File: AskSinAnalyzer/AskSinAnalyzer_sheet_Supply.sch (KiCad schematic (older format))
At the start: 8 parts, among them J1 Supply, J2 USB_B_Micro, Q1 IRLML5203, U1 LM1117-3.3

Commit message: new microUSB connector
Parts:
- J2: footprint Connectors:USB_Micro-B -> myConnectors:USB_Micro
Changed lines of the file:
@@
 F 0 "J2" H 2282 4167 50  0000 C CNN
 F 1 "USB_B_Micro" H 2282 4076 50  0000 C CNN
-F 2 "Connectors:USB_Micro-B" H 2375 3650 50  0001 C CNN
+F 2 "myConnectors:USB_Micro" H 2375 3650 50  0001 C CNN
 F 3 "~" H 2375 3650 50  0001 C CNN
 	1    2225 3700

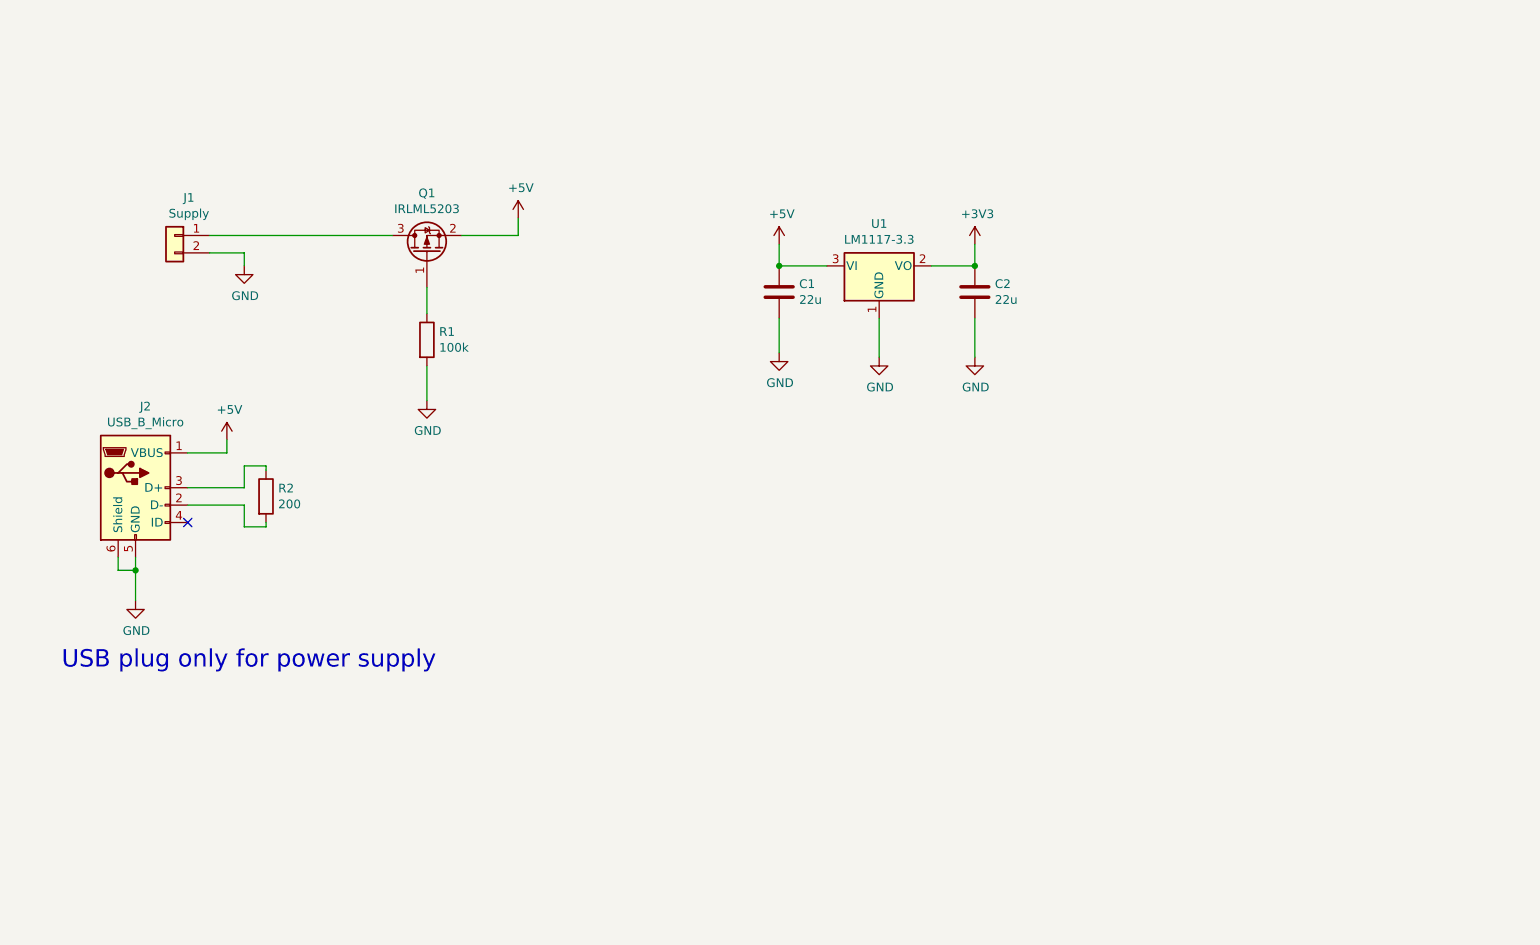
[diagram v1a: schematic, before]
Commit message: AskSinAnalyzer PCB V2.0 RC1
added a FTDI FT245 to flash and debug ESP32
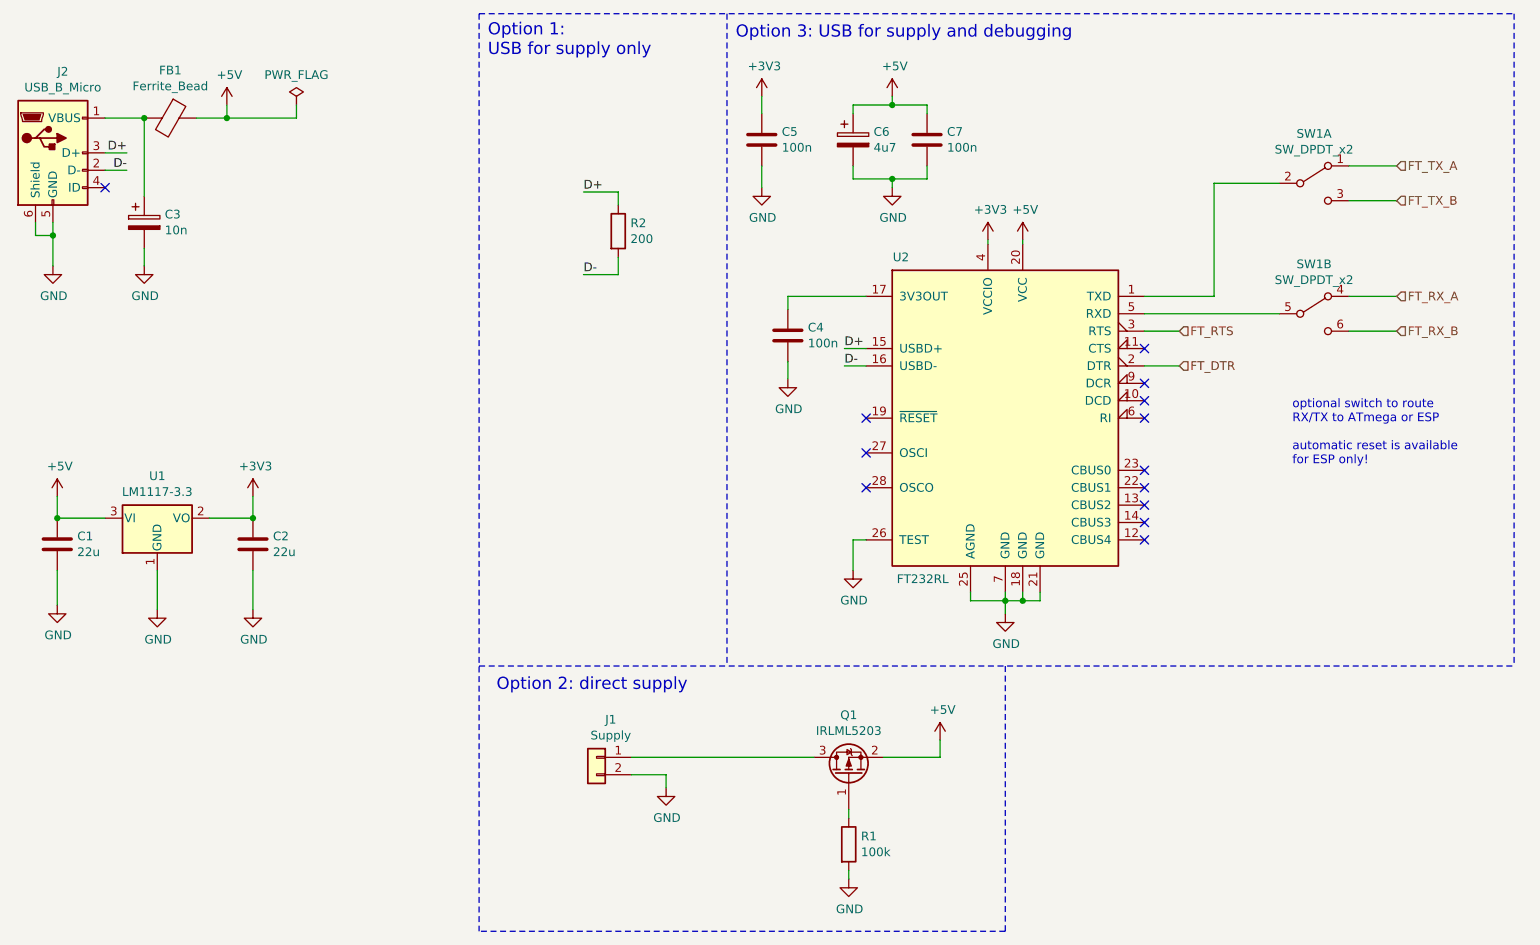
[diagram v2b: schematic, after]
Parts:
- added C3: 10n, Capacitors_SMD:C_0805_HandSoldering, symbol Device:CP
- added C4, C5: 100n, Capacitors_SMD:C_0805_HandSoldering, symbol Device:C
- added C6: 4u7, Capacitors_SMD:C_1210_HandSoldering, symbol Device:CP
- added C7: 100n, Capacitors_SMD:C_1206_HandSoldering, symbol Device:C
- added FB1: Ferrite_Bead, Resistors_SMD:R_0805_HandSoldering, symbol Device:Ferrite_Bead
- added SW1: SW_DPDT_x2, Buttons_Switches_THT:SW_CuK_JS202011CQN_DPDT_Straight, symbol Switch:SW_DPDT_x2
- added U2: FT232RL, Housings_SSOP:SSOP-28_5.3x10.2mm_Pitch0.65mm, symbol Interface_USB:FT232RL
- C1, C2: footprint Capacitors_SMD:C_1206_HandSoldering -> Capacitors_SMD:C_1210_HandSoldering
- Q1: footprint TO_SOT_Packages_SMD:SOT-23 -> TO_SOT_Packages_SMD:SOT-23_Handsoldering
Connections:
- net +3V3: now also C5.1, U2.4 (VCCIO)
- net +5V: now also C6.1, C7.1, FB1.1, U2.20 (VCC); no longer J2.1 (VBUS)
- net GND: now also C3.2, C4.2, C5.2, C6.2, C7.2, U2.18 (GND), U2.21 (GND), U2.25 (AGND), U2.26 (TEST), U2.7 (GND)
- net D-: now reaches J2.2 (D-), R2.2
- net D-: now also U2.16 (USBD-)
- net D+: now reaches J2.3 (D+), R2.1
- net D+: now also U2.15 (USBD+)
- new net: C3.1, FB1.2, J2.1 (VBUS)
- new net: SW1.2 (B), U2.1 (TXD)
- new net: C4.1, U2.17 (3V3OUT)
- new net: SW1.5 (B), U2.5 (RXD)
- new net FT_DTR: U2.2 (DTR)
- new net FT_RTS: U2.3 (RTS)
- new net FT_RX_A: SW1.4 (A)
- new net FT_RX_B: SW1.6 (C)
- new net FT_TX_A: SW1.1 (A)
- new net FT_TX_B: SW1.3 (C)
- no-connect marks 1 -> 13
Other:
- note added: "Option 1: \nUSB for supply only"
- note added: "Option 2: direct supply"
- note added: "Option 3: USB for supply and debugging\n"
- note added: "optional switch to route \nRX/TX to ATmega or ESP\n\nautomatic reset is available\nfor ESP only!\n"
- note removed: "USB plug only for power supply"
- moved on the sheet: C1, C2, J1, J2, Q1, R1, R2, U1

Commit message: AskSinAnalyzer PCB V2.0
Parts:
- C1, C2: footprint Capacitors_SMD:C_1210_HandSoldering -> Capacitors_Tantalum_SMD:CP_Tantalum_Case-B_EIA-3528-21_Hand; symbol Device:C -> Device:CP
- C3: symbol Device:CP -> Device:C
- C6: footprint Capacitors_SMD:C_1210_HandSoldering -> Capacitors_Tantalum_SMD:CP_Tantalum_Case-B_EIA-3528-21_Hand
- C7: footprint Capacitors_SMD:C_1206_HandSoldering -> Capacitors_SMD:C_0805_HandSoldering
- U2: footprint Housings_SSOP:SSOP-28_5.3x10.2mm_Pitch0.65mm -> myHousings:SSOP-28_5.3x10.2mm_Pitch0.65mm_Handsoldering
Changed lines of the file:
@@
 	6325 5900 6325 5950
 $Comp
-L Device:C C1
+L Device:CP C1
 U 1 1 5D5BA7C1
 P 1775 4025
 F 0 "C1" H 1890 4071 50  0000 L CNN
 F 1 "22u" H 1890 3980 50  0000 L CNN
-F 2 "Capacitors_SMD:C_1210_HandSoldering" H 1813 3875 50  0001 C CNN
+F 2 "Capacitors_Tantalum_SMD:CP_Tantalum_Case-B_EIA-3528-21_Hand" H 1813 3875 50  0001 C CNN
 F 3 "~" H 1775 4025 50  0001 C CNN
 	1    1775 4025
@@
 Connection ~ 1775 3875
 $Comp
-L Device:C C2
+L Device:CP C2
 U 1 1 5D5BB039
 P 2900 4025
 F 0 "C2" H 3015 4071 50  0000 L CNN
 F 1 "22u" H 3015 3980 50  0000 L CNN
-F 2 "Capacitors_SMD:C_1210_HandSoldering" H 2938 3875 50  0001 C CNN
+F 2 "Capacitors_Tantalum_SMD:CP_Tantalum_Case-B_EIA-3528-21_Hand" H 2938 3875 50  0001 C CNN
 F 3 "~" H 2900 4025 50  0001 C CNN
 	1    2900 4025
@@
 F 0 "U2" H 6625 4225 50  0000 C CNN
 F 1 "FT232RL" H 6750 2375 50  0000 C CNN
-F 2 "Housings_SSOP:SSOP-28_5.3x10.2mm_Pitch0.65mm" H 7225 3300 50  0001 C CNN
+F 2 "myHousings:SSOP-28_5.3x10.2mm_Pitch0.65mm_Handsoldering" H 7225 3300 50  0001 C CNN
 F 3 "http://www.ftdichip.com/Products/ICs/FT232RL.htm" H 7225 3300 50  0001 C CNN
 	1    7225 3300
@@
 F 1 "Ferrite_Bead" V 2242 1575 50  0000 C CNN
 F 2 "Resistors_SMD:R_0805_HandSoldering" V 2355 1575 50  0001 C CNN
-F 3 "~" H 2425 1575 50  0001 C CNN
+F 3 "Reichelt: BLM21PG 300" H 2425 1575 50  0001 C CNN
 	1    2425 1575
 	0    1    1    0
@@
 	2275 2025 2275 1575
 $Comp
-L Device:CP C3
+L Device:C C3
 U 1 1 5D5FAA20
 P 2275 2175
@@
 Wire Wire Line
 	8025 2600 8425 2600
-Text HLabel 8225 2800 2    50   Input ~ 0
-FT_RTS
 Wire Notes Line
 	5625 975  5625 4725
@@
 F 0 "C6" H 6468 1746 50  0000 L CNN
 F 1 "4u7" H 6468 1655 50  0000 L CNN
-F 2 "Capacitors_SMD:C_1210_HandSoldering" H 6388 1550 50  0001 C CNN
+F 2 "Capacitors_Tantalum_SMD:CP_Tantalum_Case-B_EIA-3528-21_Hand" H 6388 1550 50  0001 C CNN
 F 3 "~" H 6350 1700 50  0001 C CNN
 	1    6350 1700
@@
 F 0 "C7" H 6890 1746 50  0000 L CNN
 F 1 "100n" H 6890 1655 50  0000 L CNN
-F 2 "Capacitors_SMD:C_1206_HandSoldering" H 6813 1550 50  0001 C CNN
+F 2 "Capacitors_SMD:C_0805_HandSoldering" H 6813 1550 50  0001 C CNN
 F 3 "~" H 6775 1700 50  0001 C CNN
 	1    6775 1700
@@
 	3150 1575 2750 1575
 Connection ~ 2750 1575
-Wire Wire Line
-	8025 2800 8225 2800
 Text HLabel 8225 3000 2    50   Input ~ 0
 FT_DTR
@@
 Text Notes 8875 3575 0    50   ~ 0
 optional switch to route \nRX/TX to ATmega or ESP\n\nautomatic reset is available\nfor ESP only!\n
+Wire Wire Line
+	8025 2800 8225 2800
+Text HLabel 8225 2800 2    50   Input ~ 0
+FT_RTS
 $EndSCHEMATC

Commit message: add production data to AskSinAnalyzer PCB
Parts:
- C1, C2: LCSC (none) -> C110051
- C3: LCSC (none) -> C1710
- C4, C5, C6, C7: Option (none) -> 3_USB_debugging
- FB1: LCSC (none) -> C16903
- J1, J2: LCSC (none) -> -
- Q1: LCSC (none) -> C2592; Option (none) -> 2_direct_supply
- R1: LCSC (none) -> C17407; Option (none) -> 2_direct_supply
- R2: LCSC (none) -> C17540; Option (none) -> 1_USB_for_supply_only
- SW1, U2: LCSC (none) -> -; Option (none) -> 3_USB_debugging
- U1: LCSC (none) -> C23984
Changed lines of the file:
@@
 F 2 "TO_SOT_Packages_SMD:SOT-223" H 2350 3875 50  0001 C CNN
 F 3 "http://www.ti.com/lit/ds/symlink/lm1117.pdf" H 2350 3875 50  0001 C CNN
+F 4 "C23984" H 2350 3875 50  0001 C CNN "LCSC"
 	1    2350 3875
 	1    0    0    -1
@@
 F 2 "TO_SOT_Packages_SMD:SOT-23_Handsoldering" H 6525 5450 50  0001 C CNN
 F 3 "~" H 6325 5350 50  0001 C CNN
+F 4 "2_direct_supply" V 6325 5350 50  0001 C CNN "Option"
+F 5 "C2592" H 6325 5350 50  0001 C CNN "LCSC"
 	1    6325 5350
 	0    -1   -1   0
@@
 F 2 "Capacitors_Tantalum_SMD:CP_Tantalum_Case-B_EIA-3528-21_Hand" H 1813 3875 50  0001 C CNN
 F 3 "~" H 1775 4025 50  0001 C CNN
+F 4 "C110051" H 1775 4025 50  0001 C CNN "LCSC"
 	1    1775 4025
 	1    0    0    -1
@@
 F 2 "Capacitors_Tantalum_SMD:CP_Tantalum_Case-B_EIA-3528-21_Hand" H 2938 3875 50  0001 C CNN
 F 3 "~" H 2900 4025 50  0001 C CNN
+F 4 "C110051" H 2900 4025 50  0001 C CNN "LCSC"
 	1    2900 4025
 	1    0    0    -1
@@
 F 2 "myConnectors:USB_Micro" H 1900 1725 50  0001 C CNN
 F 3 "~" H 1900 1725 50  0001 C CNN
+F 4 "-" H 1750 1775 50  0001 C CNN "LCSC"
 	1    1750 1775
 	1    0    0    -1
@@
 F 2 "Pin_Headers:Pin_Header_Straight_1x02_Pitch2.54mm" H 4875 5250 50  0001 C CNN
 F 3 "~" H 4875 5250 50  0001 C CNN
+F 4 "-" H 4875 5250 50  0001 C CNN "LCSC"
 	1    4875 5250
 	-1   0    0    -1
@@
 F 2 "Resistors_SMD:R_0805_HandSoldering" V 4930 2225 50  0001 C CNN
 F 3 "~" H 5000 2225 50  0001 C CNN
+F 4 "1_USB_for_supply_only" H 5000 2225 50  0001 C CNN "Option"
+F 5 "C17540" H 5000 2225 50  0001 C CNN "LCSC"
 	1    5000 2225
 	1    0    0    -1
@@
 F 2 "myHousings:SSOP-28_5.3x10.2mm_Pitch0.65mm_Handsoldering" H 7225 3300 50  0001 C CNN
 F 3 "http://www.ftdichip.com/Products/ICs/FT232RL.htm" H 7225 3300 50  0001 C CNN
+F 4 "3_USB_debugging" H 7225 3300 50  0001 C CNN "Option"
+F 5 "-" H 7225 3300 50  0001 C CNN "LCSC"
 	1    7225 3300
 	1    0    0    -1
@@
 F 2 "Resistors_SMD:R_0805_HandSoldering" V 6255 5750 50  0001 C CNN
 F 3 "~" H 6325 5750 50  0001 C CNN
+F 4 "2_direct_supply" H 6325 5750 50  0001 C CNN "Option"
+F 5 "C17407" H 6325 5750 50  0001 C CNN "LCSC"
 	1    6325 5750
 	1    0    0    -1
@@
 F 2 "Resistors_SMD:R_0805_HandSoldering" V 2355 1575 50  0001 C CNN
 F 3 "Reichelt: BLM21PG 300" H 2425 1575 50  0001 C CNN
+F 4 "C16903" H 2425 1575 50  0001 C CNN "LCSC"
 	1    2425 1575
 	0    1    1    0
@@
 F 2 "Capacitors_SMD:C_0805_HandSoldering" H 2313 2025 50  0001 C CNN
 F 3 "~" H 2275 2175 50  0001 C CNN
+F 4 "C1710" H 2275 2175 50  0001 C CNN "LCSC"
 	1    2275 2175
 	1    0    0    -1
@@
 F 2 "Capacitors_SMD:C_0805_HandSoldering" H 6013 2675 50  0001 C CNN
 F 3 "~" H 5975 2825 50  0001 C CNN
+F 4 "3_USB_debugging" H 5975 2825 50  0001 C CNN "Option"
 	1    5975 2825
 	1    0    0    -1
@@
 F 2 "Capacitors_Tantalum_SMD:CP_Tantalum_Case-B_EIA-3528-21_Hand" H 6388 1550 50  0001 C CNN
 F 3 "~" H 6350 1700 50  0001 C CNN
+F 4 "3_USB_debugging" H 6350 1700 50  0001 C CNN "Option"
 	1    6350 1700
 	1    0    0    -1
@@
 F 2 "Capacitors_SMD:C_0805_HandSoldering" H 6813 1550 50  0001 C CNN
 F 3 "~" H 6775 1700 50  0001 C CNN
+F 4 "3_USB_debugging" H 6775 1700 50  0001 C CNN "Option"
 	1    6775 1700
 	1    0    0    -1
@@
 F 2 "Capacitors_SMD:C_0805_HandSoldering" H 5863 1550 50  0001 C CNN
 F 3 "~" H 5825 1700 50  0001 C CNN
+F 4 "3_USB_debugging" H 5825 1700 50  0001 C CNN "Option"
 	1    5825 1700
 	1    0    0    -1
@@
 F 2 "Buttons_Switches_THT:SW_CuK_JS202011CQN_DPDT_Straight" H 9000 1950 50  0001 C CNN
 F 3 "~" H 9000 1950 50  0001 C CNN
+F 4 "3_USB_debugging" H 9000 1950 50  0001 C CNN "Option"
+F 5 "-" H 9000 1950 50  0001 C CNN "LCSC"
 	1    9000 1950
 	1    0    0    -1
@@
 F 2 "Buttons_Switches_THT:SW_CuK_JS202011CQN_DPDT_Straight" H 9000 2700 50  0001 C CNN
 F 3 "~" H 9000 2700 50  0001 C CNN
+F 4 "3_USB_debugging" H 9000 2700 50  0001 C CNN "Option"
+F 5 "-" H 9000 2700 50  0001 C CNN "LCSC"
 	2    9000 2700
 	1    0    0    -1
